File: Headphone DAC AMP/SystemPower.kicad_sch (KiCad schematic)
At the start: 34 parts, among them U1 NCV8187AMTW090TAG, U11 ADP5071AREZ-R7, U6 MCP1727-1802xSN, U7 MCP1727-3302xSN

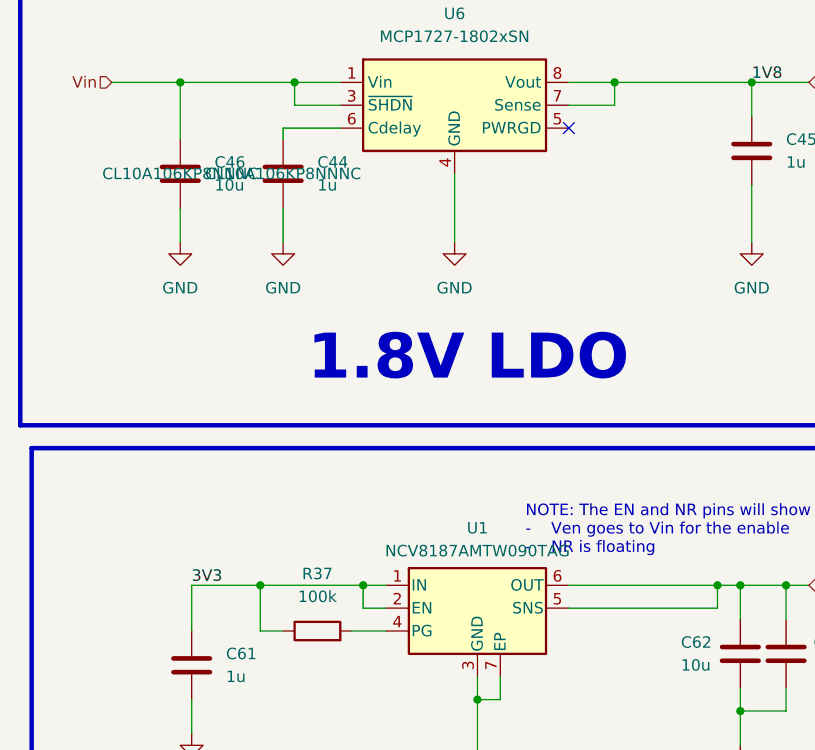
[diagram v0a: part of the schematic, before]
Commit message: Update PCB layout
Updated component properties and positions in Headphone DAC AMP.kicad_pcb, including changes to reference designators, datasheet fields, and footprint coordinates for several resistors and capacitors.
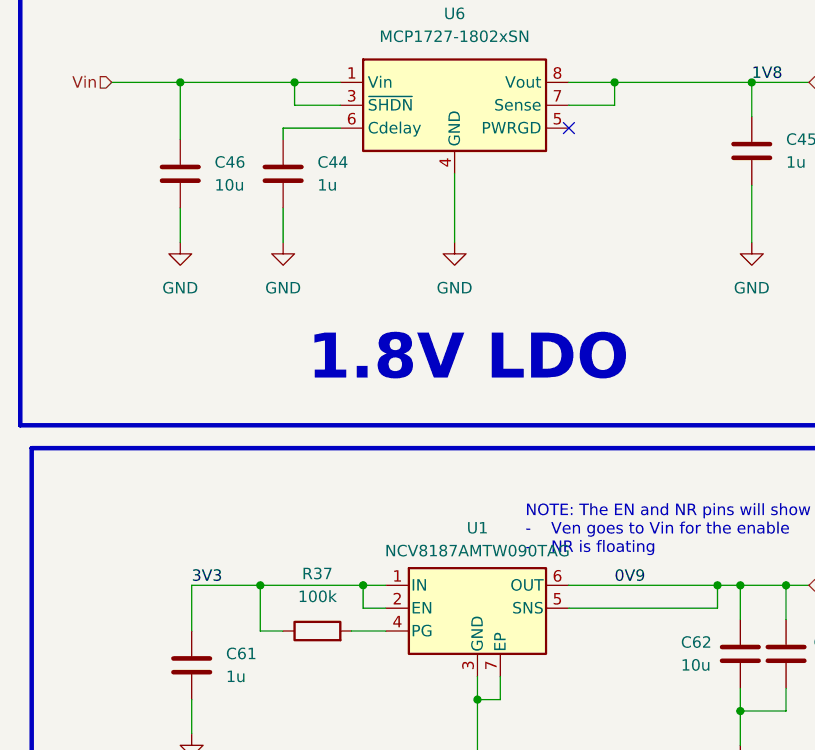
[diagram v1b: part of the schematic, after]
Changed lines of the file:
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@@
 	)
 	(junction
-		(at 165.1 41.91)
+		(at 99.06 148.59)
 		(diameter 0)
 		(color 0 0 0 0)
 	)
 	(junction
-		(at 99.06 148.59)
+		(at 165.1 41.91)
 		(diameter 0)
 		(color 0 0 0 0)
@@
 	(wire
 		(pts
-			(xy 82.55 151.13) (xy 99.06 151.13)
-		)
-		(stroke
-			(width 0)
-			(type default)
-		)
-	)
-	(wire
-		(pts
 			(xy 106.68 148.59) (xy 109.22 148.59)
 		)
@@
 	(wire
 		(pts
-			(xy 82.55 148.59) (xy 99.06 148.59)
-		)
-		(stroke
-			(width 0)
-			(type default)
-		)
-	)
-	(wire
-		(pts
 			(xy 165.1 44.45) (xy 165.1 41.91)
 		)
@@
 	(wire
 		(pts
+			(xy 82.55 151.13) (xy 99.06 151.13)
+		)
+		(stroke
+			(width 0)
+			(type default)
+		)
+	)
+	(wire
+		(pts
 			(xy 173.99 35.56) (xy 173.99 39.37)
 		)
@@
 	(wire
 		(pts
+			(xy 82.55 148.59) (xy 99.06 148.59)
+		)
+		(stroke
+			(width 0)
+			(type default)
+		)
+	)
+	(wire
+		(pts
 			(xy 74.93 161.29) (xy 72.39 161.29)
 		)
@@
 		)
 	)
+	(label "0V9"
+		(at 87.63 148.59 0)
+		(effects
+			(font
+				(size 1.27 1.27)
+			)
+			(justify left bottom)
+		)
+	)
 	(label "VREG"
 		(at 171.45 46.99 180)
@@
 					(size 1.27 1.27)
 				)
+				(hide yes)
 			)
 		)
@@
 		)
 		(instances
-			(project ""
+			(project "Headphone DAC AMP"
 				(path "/d034eddd-efbc-47be-a25c-37cbfbab4cd8/a76b11f7-fbf9-4331-be15-052b46a69f96"
 					(reference "U1")
@@
 					(size 1.27 1.27)
 				)
+				(hide yes)
 			)
 		)

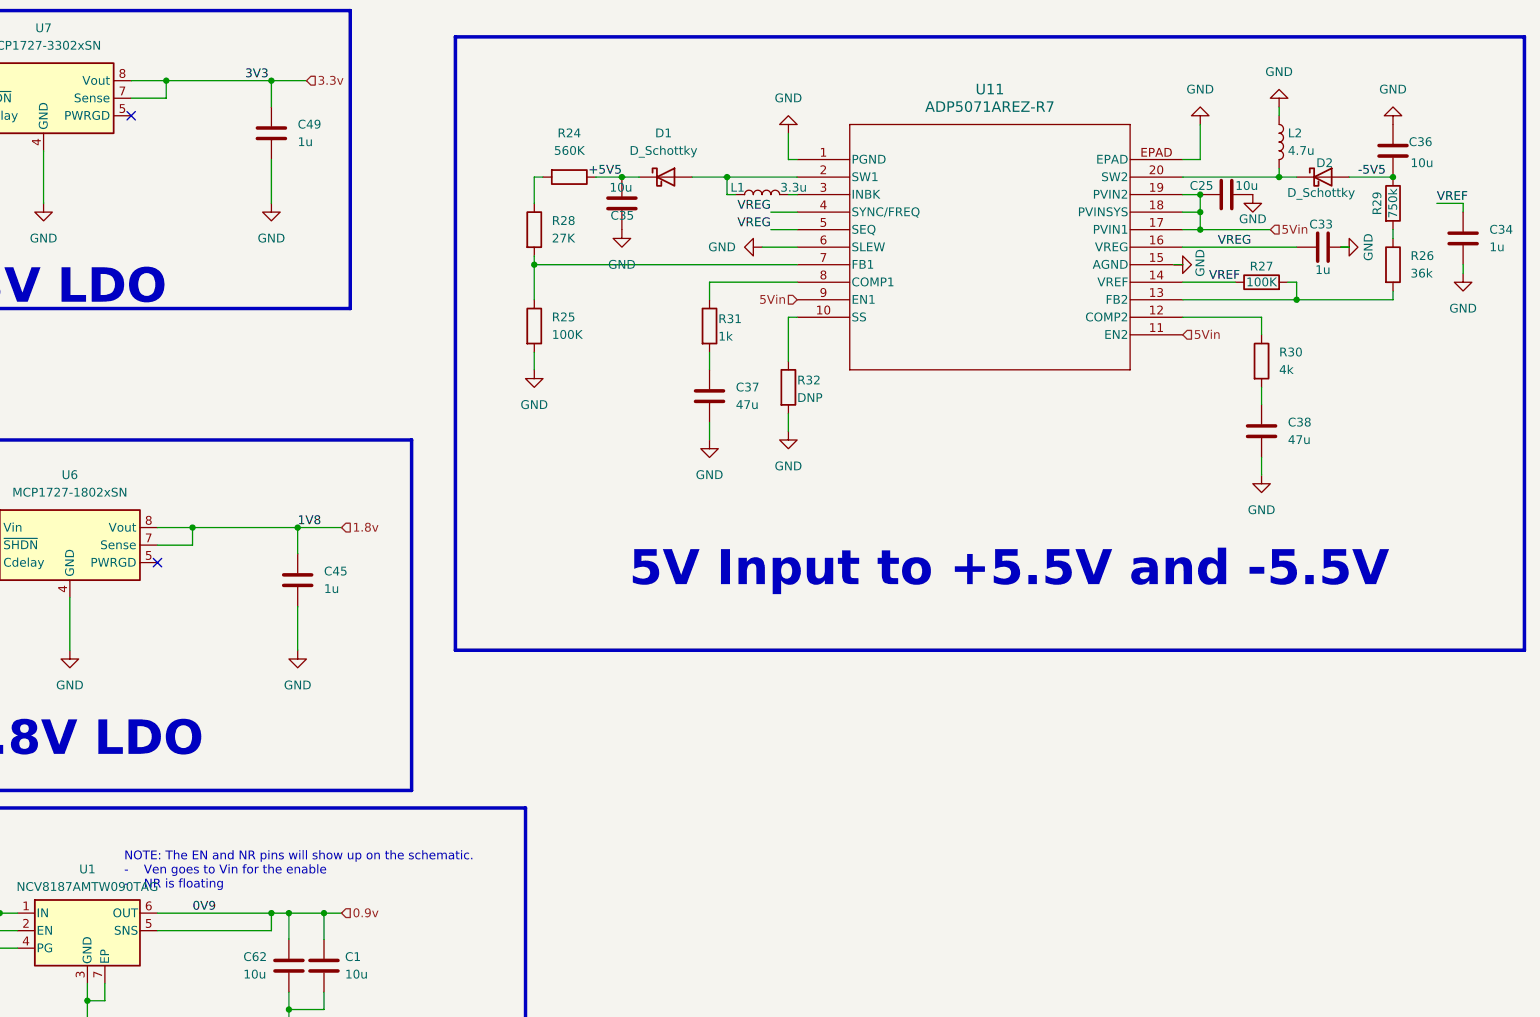
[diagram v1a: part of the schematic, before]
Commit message: +-6V conversion Update SystemPower schematic
Updated SystemPower.kicad_sch with updated ADP5071 Values, new voltage text, removed a note, added new junctions and wires, and inserted an image. Modified DRC exclusions in Headphone DAC AMP.kicad_pro.
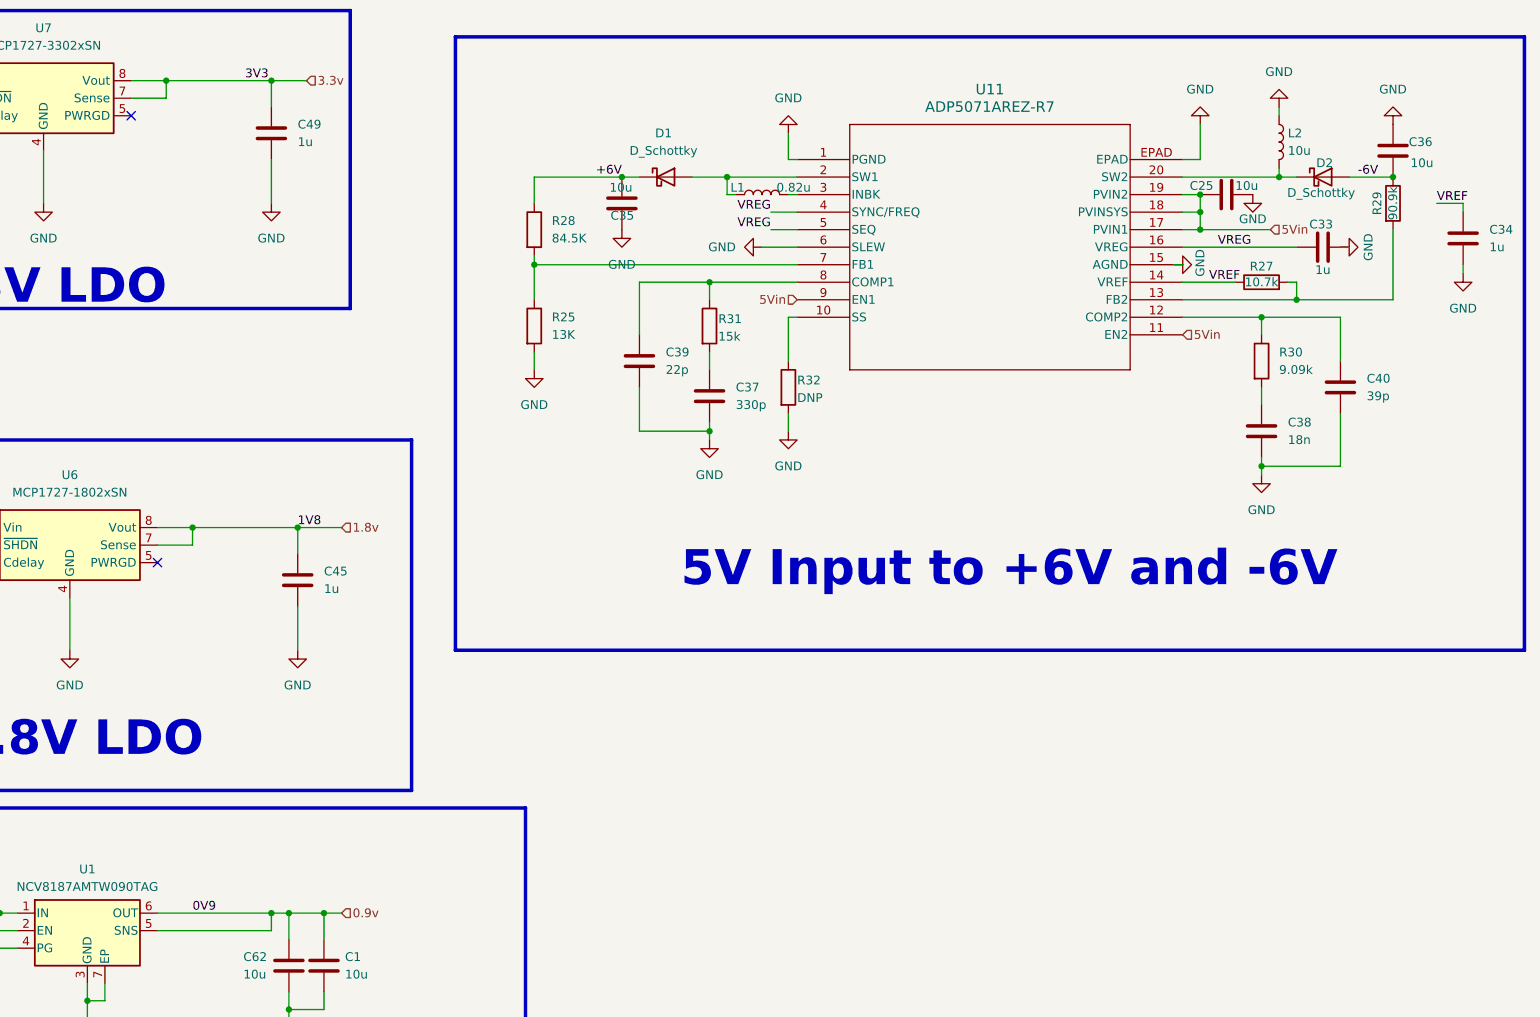
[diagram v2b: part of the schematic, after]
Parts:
- removed R24: 560K, Resistor_SMD:R_0805_2012Metric_Pad1.20x1.40mm_HandSolder, symbol Device:R
- removed R26: 36k, Resistor_SMD:R_0805_2012Metric_Pad1.20x1.40mm_HandSolder, symbol Device:R
- added C39: 22p, Capacitor_SMD:C_0603_1608Metric_Pad1.08x0.95mm_HandSolder, symbol Device:C
- added C40: 39p, Capacitor_SMD:C_0603_1608Metric_Pad1.08x0.95mm_HandSolder, symbol Device:C
- C37: value 47u -> 330p
- C38: value 47u -> 18n
- L1: value 3.3u -> 0.82u
- L2: value 4.7u -> 10u
- R25: value 100K -> 13K
- R27: value 100K -> 10.7k
- R28: value 27K -> 84.5K
- R29: value 750k -> 90.9k
- R30: value 4k -> 9.09k
- R31: value 1k -> 15k
- U1: footprint Package_SON:WSON-6-1EP_3x3mm_P0.95mm -> NCV8187AMTW090TAG:SON65P200X200X80-7N
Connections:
- net +5V5 is gone; now on net +6V: C35.2, D1.1 (K)
- net GND: now also C39.2, C40.2
- net at R31.1, U11.8 (COMP1): now also C39.1
- net at R27.2, U11.13 (FB2): now also R29.2
- net at R30.1, U11.12 (COMP2): now also C40.1
- net +6V: now reaches R28.1
- net -5V5 renamed -6V
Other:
- note added: "5V Input to +6V and -6V"
- note removed: "5V Input to +5.5V and -5.5V"
- note removed: "NOTE: The EN and NR pins will show up on the schematic. - Ven goes to Vin for the enable - NR is floating"

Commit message: Worked on layout briefley
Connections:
- net 3.3v: no longer U1.6 (OUT)
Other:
- moved on the sheet: C1, C25, C33, C34, C35, C36, C37, C38, C39, C40, C44, C45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
